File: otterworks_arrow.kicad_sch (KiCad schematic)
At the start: 1 part, among them U1 STM32F030C6Tx

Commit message: bottom side done
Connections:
- net leds1/DIN: now reaches U1.29 (PA8)
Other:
- added sheet leds1 (leds.kicad_sch)
- note added: "TODO - accel / gyro - ambient light detector - battery level"
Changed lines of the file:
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@@
+		)
+	)
+	(wire
+		(pts
+			(xy 64.77 104.14) (xy 107.95 104.14)
+		)
+		(stroke
+			(width 0)
+			(type default)
+		)
+	)
+	(text "TODO\n- accel / gyro\n- ambient light detector\n- battery level"
+		(exclude_from_sim no)
+		(at 24.13 32.004 0)
+		(effects
+			(font
+				(size 3.81 3.81)
+			)
+			(justify left)
 		)
 	)
@@
 				)
 			)
+		)
+	)
+	(sheet
+		(at 107.95 96.52)
+		(size 26.035 15.24)
+		(fields_autoplaced yes)
+		(stroke
+			(width 0.1524)
+			(type solid)
+		)
+		(fill
+			(color 0 0 0 0.0000)
+		)
+		(property "Sheetname" "leds1"
+			(at 107.95 95.8084 0)
+			(effects
+				(font
+					(size 1.27 1.27)
+				)
+				(justify left bottom)
+			)
+		)
+		(property "Sheetfile" "leds.kicad_sch"
+			(at 107.95 112.3446 0)
+			(effects
+				(font
+					(size 1.27 1.27)
+				)
+				(justify left top)
+			)
+		)
+		(pin "DOUT" output
+			(at 133.985 104.14 0)
+			(effects
+				(font
+					(size 1.27 1.27)
+				)
+				(justify right)
+			)
+		)
+		(pin "DIN" input
+			(at 107.95 104.14 180)
+			(effects
+				(font
+					(size 1.27 1.27)
+				)
+				(justify left)
+			)
+		)
+		(instances
+			(project "otterworks_arrow"
+				(path "/4b10177f-59fb-4d44-b63c-4086913e7acb"
+					(page "71")
+				)
+			)

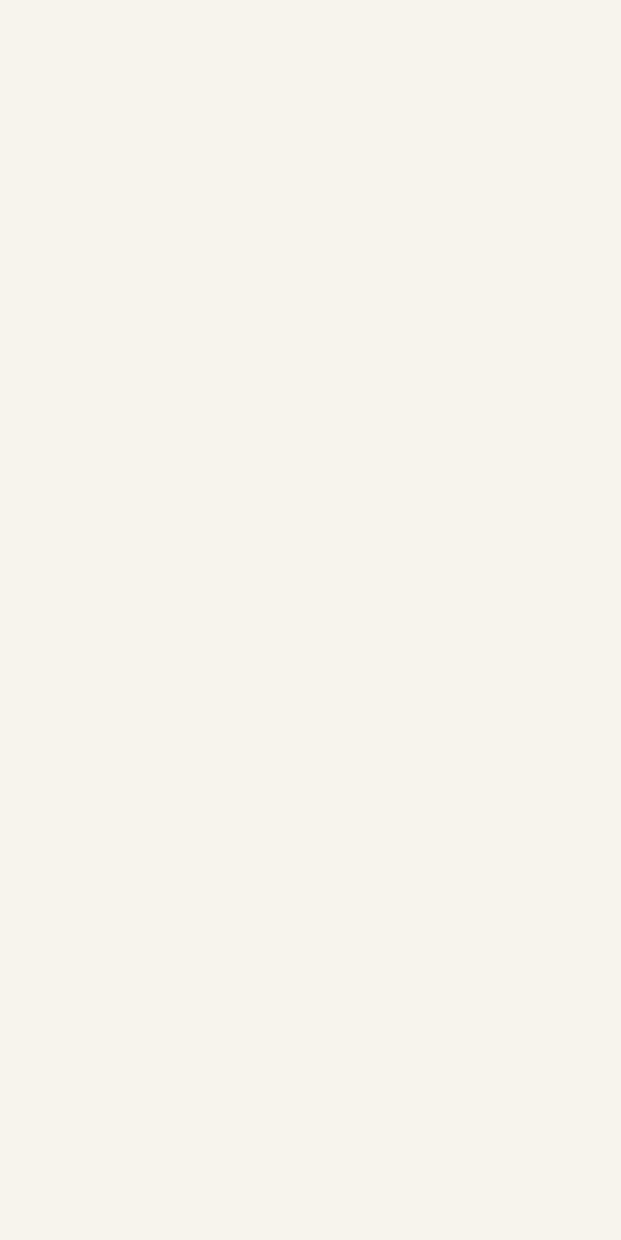
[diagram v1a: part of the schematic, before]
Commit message: bosh IMU addded
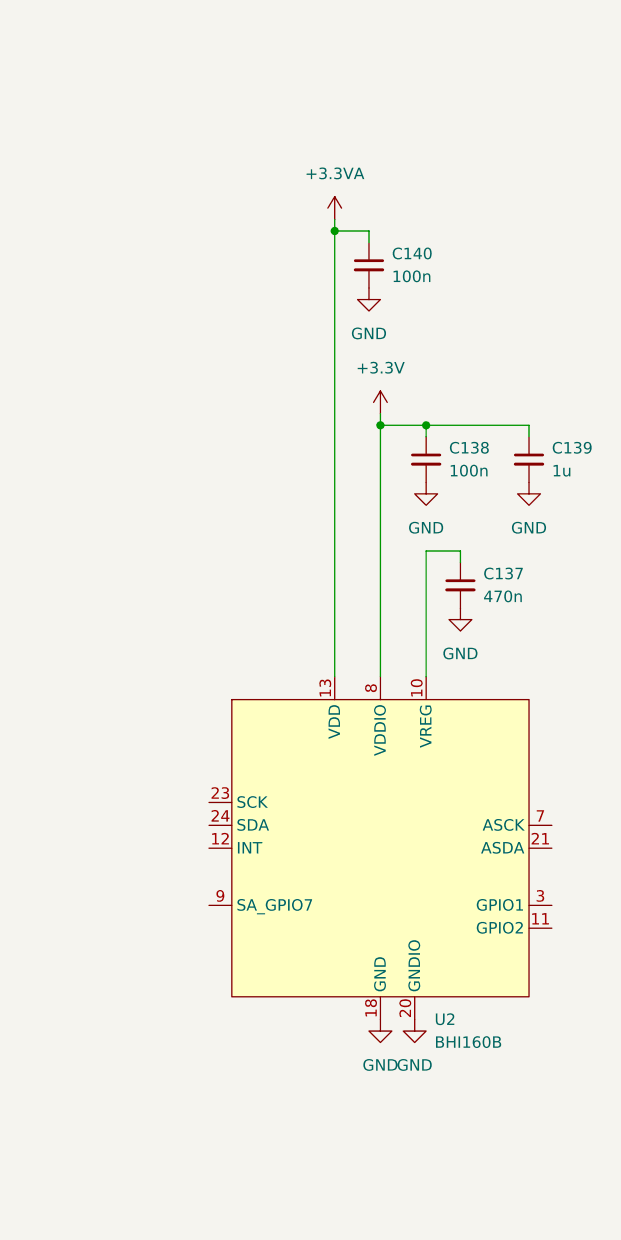
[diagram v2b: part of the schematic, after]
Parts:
- added C137: 470n, Capacitor_SMD:C_0603_1608Metric, symbol Device:C_Small
- added C138, C140: 100n, Capacitor_SMD:C_0603_1608Metric, symbol Device:C_Small
- added C139: 1u, Capacitor_SMD:C_0603_1608Metric, symbol Device:C_Small
- added U2: BHI160B, LGA24_3x3:LGA-24_3x3mm, symbol bosch:BHI160(B)
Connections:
- new net: C137.1, U2.10 (VREG)
- new net: U2.1 (NC), U2.14 (NC), U2.15 (NC), U2.16 (NC), U2.17 (NC), U2.19 (NC), U2.2 (DNC), U2.22 (RESV4), U2.4 (RESV2), U2.5 (RESV3), U2.6 (NC)
- new net +3.3V: C138.1, C139.1, U2.8 (VDDIO)
- new net +3.3VA: C140.1, U2.13 (VDD)
- new net GND: C137.2, C138.2, C139.2, C140.2, U2.18 (GND), U2.20 (GNDIO)

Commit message: wip
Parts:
- removed U1: STM32F030C6Tx, Package_QFP:LQFP-48_7x7mm_P0.5mm, symbol MCU_ST_STM32F0:STM32F030C6Tx
- added C141, C142, C143, C144: 100n, Capacitor_SMD:C_0603_1608Metric, symbol Device:C_Small
- added FB1: ferrite, Inductor_SMD:L_0603_1608Metric, symbol Device:FerriteBead_Small
- added J1: PROG, Connector_PinHeader_2.54mm:PinHeader_1x06_P2.54mm_Vertical, symbol Connector:Conn_01x06_Socket
- added R1, R10, R11, R12: 0, Resistor_SMD:R_0603_1608Metric, symbol Device:R_Small
- added R13, R14, R2, R3: 10k, Resistor_SMD:R_0603_1608Metric, symbol Device:R_Small
- added R4, R5, R6, R7: 100, Resistor_SMD:R_0603_1608Metric, symbol Device:R_Small
- added R8, R9: 2.2k, Resistor_SMD:R_0603_1608Metric, symbol Device:R_Small
- added SW1: SW_Push, Button_Switch_SMD:SW_Push_1P1T_NO_CK_KSC7xxJ, symbol Switch:SW_Push
- added TP0, TP1, TP2, TP3, TP4, TP5, TP6, TP7, TP8: TestPoint, TestPoint:TestPoint_Pad_D1.0mm, symbol Connector:TestPoint
- added U3: STM32F030K6Tx, Package_QFP:LQFP-32_7x7mm_P0.8mm, symbol MCU_ST_STM32F0:STM32F030K6Tx
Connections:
- net +3.3V: now also FB1.1, R13.1, R3.1, R8.1, R9.1
- net GND: now also C141.2, C142.2, C143.2, C144.2, J1.1 (Pin_1), R2.2, SW1.2, U3.16 (VSS), U3.32 (VSS)
- net leds/DIN: now also R1.1, R10.1, R11.1
- net leds1/DIN: now also R1.2, R12.1
- net I2C1_INT: now reaches U2.12 (INT)
- net I2C1_INT: now also TP5.1, U3.28 (PB5)
- net I2C1_SCL: now reaches U2.23 (SCK)
- net I2C1_SCL: now also R8.2, R9.2, TP3.1, U3.29 (PB6)
- net I2C1_SDA: now reaches U2.24 (SDA)
- net I2C1_SDA: now also TP4.1, U3.30 (PB7)
- new net: J1.2 (Pin_2), R4.1
- new net: J1.5 (Pin_5), R6.1
- new net: J1.4 (Pin_4), R5.1
- new net: C141.1, C142.1, C143.1, FB1.2, U3.1 (VDD), U3.17 (VDD), U3.5 (VDDA)
- new net: C144.1, R14.1, U3.9 (PA3)
- new net: R13.2, R14.2, SW1.1
- new net: J1.6 (Pin_6), R7.1
- new net PROG_BOOT0: R2.1, R7.2, U3.31 (BOOT0)
- new net PROG_NRST: R3.2, R4.2, U3.4 (NRST)
- new net PROG_RX: R5.2, U3.20 (PA10)
- new net PROG_TX: R6.2, U3.19 (PA9)
- new net SPI1_MOSI: R11.2, TP6.1, U3.13 (PA7)
- new net TIM3_CH3: R10.2, TP7.1, U3.14 (PB0)
- new net TIM3_CH4: R12.2, TP8.1, U3.15 (PB1)
- new net TP0: TP0.1, U3.6 (PA0)
- new net TP1: TP1.1, U3.7 (PA1)
- new net TP2: TP2.1, U3.8 (PA2)
- no-connect marks 0 -> 18
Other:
- note added: "TODO X accel / gyro - ambient light detector - battery level - switch"
- note removed: "TODO - accel / gyro - ambient light detector - battery level"
- moved on the sheet: C137, C138, C139, C140, U2

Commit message: wip
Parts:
- added C146, C147, C148: 100n, Capacitor_SMD:C_0603_1608Metric, symbol Device:C_Small
- added D137: BPW34, OptoDevice:Osram_DIL2_4.3x4.65mm_P5.08mm, symbol Sensor_Optical:BPW34
- added FB2: ferrite, Inductor_SMD:L_0603_1608Metric, symbol Device:FerriteBead_Small
- added H1, H2: MountingHole_Pad, MountingHole:MountingHole_3.2mm_M3_Pad, symbol Mechanical:MountingHole_Pad
- added H3, H4: MountingHole, MountingHole:MountingHole_6mm, symbol Mechanical:MountingHole
- added P1: USB_C_Plug_USB2.0, Connector_USB:USB_C_Receptacle_HRO_TYPE-C-31-M-12, symbol Connector:USB_C_Plug_USB2.0
- added Q1: MMBT2484LT1G, Package_TO_SOT_SMD:SOT-23, symbol Device:Q_NPN_BEC
- added R15, R16: 5.1k, Resistor_SMD:R_0603_1608Metric, symbol Device:R_Small
- added R17: 0, Resistor_SMD:R_0603_1608Metric, symbol Device:R_Small
- added R18, R21: 33k, Resistor_SMD:R_0603_1608Metric, symbol Device:R_Small
- added R19, R22, R23: 10k, Resistor_SMD:R_0603_1608Metric, symbol Device:R_Small
- added R20: 10, Resistor_SMD:R_0603_1608Metric, symbol Device:R_Small
- added U1: ADP7142AUJZ-3.3, Package_TO_SOT_SMD:TSOT-23-5, symbol Regulator_Linear:ADP7142AUJZ-3.3
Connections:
- net +3.3V: now also C147.1, D137.1 (K), FB2.1, R17.2, R20.2, U1.5 (VOUT)
- net GND: now also C146.2, C147.2, C148.2, H1.1, H2.1, P1.A1 (GND), P1.A12 (GND), P1.B1 (GND), P1.B12 (GND), P1.S1 (SHIELD), Q1.2 (E), R15.2, R16.2, R19.1, R22.1, U1.2 (GND)
- net I2C1_SCL: no longer R9.2
- net I2C1_SDA: now also R9.2
- net IN_SWITCH: now reaches C144.1, R14.1, U3.9 (PA3)
- net IN_ADC_SUPPLY: now reaches U3.10 (PA4)
- net IN_ADC_SUPPLY: now also R18.1, R19.2
- net IN_AMB_LIGHT: now reaches U3.11 (PA5)
- net IN_AMB_LIGHT: now also C148.1, R21.1, R22.2
- net +3.3VA: no longer names the net of C140.1, U2.13 (VDD)
- net +3.3VA: now also FB2.2
- new net: P1.A5 (CC), R16.1
- new net: P1.B5 (VCONN), R15.1
- new net: R23.2, U1.3 (EN)
- new net: Q1.3 (C), R20.1, R21.2
- new net: D137.2 (A), Q1.1 (B)
- new net: R17.1, U1.4 (SENSE/ADJ)
- new net +5V: C146.1, P1.A4 (VBUS), P1.A9 (VBUS), P1.B4 (VBUS), P1.B9 (VBUS), R18.2, R23.1, U1.1 (VIN)
- no-connect marks 18 -> 19
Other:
- note added: "TODO X accel / gyro - ambient light detector X battery level X switch"
- note removed: "TODO X accel / gyro - ambient light detector - battery level - switch"
- moved on the sheet: C140, C141, C142, C143, C144, FB1, R13, R14, R2, R3, SW1, U3
